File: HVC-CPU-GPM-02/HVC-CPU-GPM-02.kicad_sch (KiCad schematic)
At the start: 31 parts, among them P1 CART, P3 RF, P6 POWER, Q1 2SA937, SW1 RESET, U1 MB8416, U2 74LS373, U3 74LS139, U4 MB8416, U5 RP2C02, U6 RP2A03

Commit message: Refactor schematic: * Move audio and video circuits to dedicated sheet * Move power and mechanical to dedicated sheet Modify P1 Cart Connector symbol to: * split out audio ports * organize pins for easier wiring Modify 74LS346 symbol: * Split A/B ports to allow moving functions to related circuits Modify X1 crystal footprint: * change from stock footprint to custom footprint Correct crystal name from Y1 to X1
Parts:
- removed C10, C35: 0.01u, Nintendo:C_Disc_D3.0mm_W2.0mm_P3.0mm, symbol Device:C
- removed C34, C40, C41, C42, C43, C44, C45, C46: 330p, Nintendo:C_Disc_D3.0mm_W2.0mm_P3.0mm, symbol Device:C
- removed C8: 0.47u, Capacitor_THT:CP_Radial_D5.0mm_P2.50mm, symbol Device:C_Polarized
- removed FC1: 39u, Inductor_THT:L_Axial_L5.0mm_D3.6mm_P10.00mm_Horizontal_Murata_BL01RN1A2A2, symbol Device:L_Ferrite
- removed FC2: FerriteBead, Inductor_THT:L_Axial_L5.0mm_D3.6mm_P10.00mm_Horizontal_Murata_BL01RN1A2A2, symbol Device:FerriteBead
- removed H1: Top Left, Nintendo:npth_mounting_4x5mm_pad, symbol Mechanical:MountingHole_Pad
- removed H2: Top Right, Nintendo:npth_mounting_4x5mm_nopad, symbol Mechanical:MountingHole
- removed H3: Bottom Left, Nintendo:npth_mounting_3.3x5mm_nopad, symbol Mechanical:MountingHole
- removed H4: Bottom Right, Nintendo:npth_mounting_3.3x5mm_nopad, symbol Mechanical:MountingHole
- removed H5: Alignment, Nintendo:npth_mounting_2x4mm_nopad, symbol Mechanical:MountingHole
- removed P6: POWER, Nintendo:connector_P6_2pin, symbol Switch:SW_SPST
- removed Q1: 2SA937, Nintendo:PACKAGE_TRANSISTOR_FTR, symbol Simulation_SPICE:PNP
- removed R6: 150, Resistor_THT:R_Axial_DIN0207_L6.3mm_D2.5mm_P10.16mm_Horizontal, symbol Device:R
- removed SW1: RESET, Nintendo:switch_reset_9x10_4pin, symbol Switch:SW_Push_Dual
- removed unit 3 of U3
- added C37, C38: 560p, Nintendo:C_Disc_D3.0mm_W2.0mm_P3.0mm, symbol Device:C
- P1: value CART -> CARTRIGE SLOT
- P3: value RF -> RF MODULATOR; symbol Connector:Conn_01x05_Socket -> Famicom:RF_MODULATOR
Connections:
- net GND: now also C37.2, C38.2
- net SOUND+CART: no longer P1.46 (SNDO)
- net ~{INP0}: now also C38.1
- net ~{INP1}: now also C37.1
- net AUDIO renamed RF_AUDIO
- net Clock/CPU_CLK renamed CPU_CLK
- net Clock/PPU_CLK renamed PPU_CLK
- net POWER_IN renamed POWER
- net SND1 renamed CPU_SND1
- net SND2 renamed CPU_SND2
- removed net SOUND: P1.45 (SNDI)
- net VIDEO renamed PPU_VIDEO
- net VID_AF renamed RF_VIDEO
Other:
- sheet Audio renamed Audio and Video
- added sheet Power and Mechanical (power_mech.kicad_sch)
- sheet Audio and Video ports: added CPU_SND1, CPU_SND2, MIC, PA13, PPU_VIDEO, RF_AUDIO, RF_VIDEO, SOUND+CART, ~{PA13}; removed none
- sheet Controllers ports: added none; removed PA13, SND1, SND2, SOUND, ~{PA13}
- note added: "1 2 3 4 5 6 7 8 9 10 11 12 13 14 15 16 17 18 19 20 21 22 23 24 25 26 27 28 29 30"
- note added: "31 32 33 34 35 36 37 38 39 40 41 42 43 44 45 46 47 48 49 50 51 52 53 54 55 56 57 58 59 60"
- note added: "ADDRESS LATCH"
- note added: "CPU"
- note added: "GND A11 A10 A9 A8 A7 A6 A5 A4 A3 A2 A1 A0 R/~{W} ~{IRQ} GND ~{RD} VA10 PA6 PA5 PA4 PA3 PA2 PA1 PA0 PD0 PD1 PD2 PD3 VCC"
- note added: "POWER"
- note added: "RESET"
- note added: "RF_VCC M2 A12 A13 A14 D7 D6 D5 D4 D3 D2 D1 D0 ~{ROMSEL} SNDI SNDO ~{WE} ~{VCS} ~{PA13} PA7 PA8 PA9 PA10 PA11 PA12 PA13 PD7 PD6 PD5 PD4"
- note removed: "INDUCTORS 39uH x1 Ferrite x1"
- moved on the sheet: RM1F, RM1G, U1, U2, U3A, U3B, U4, U5, U6

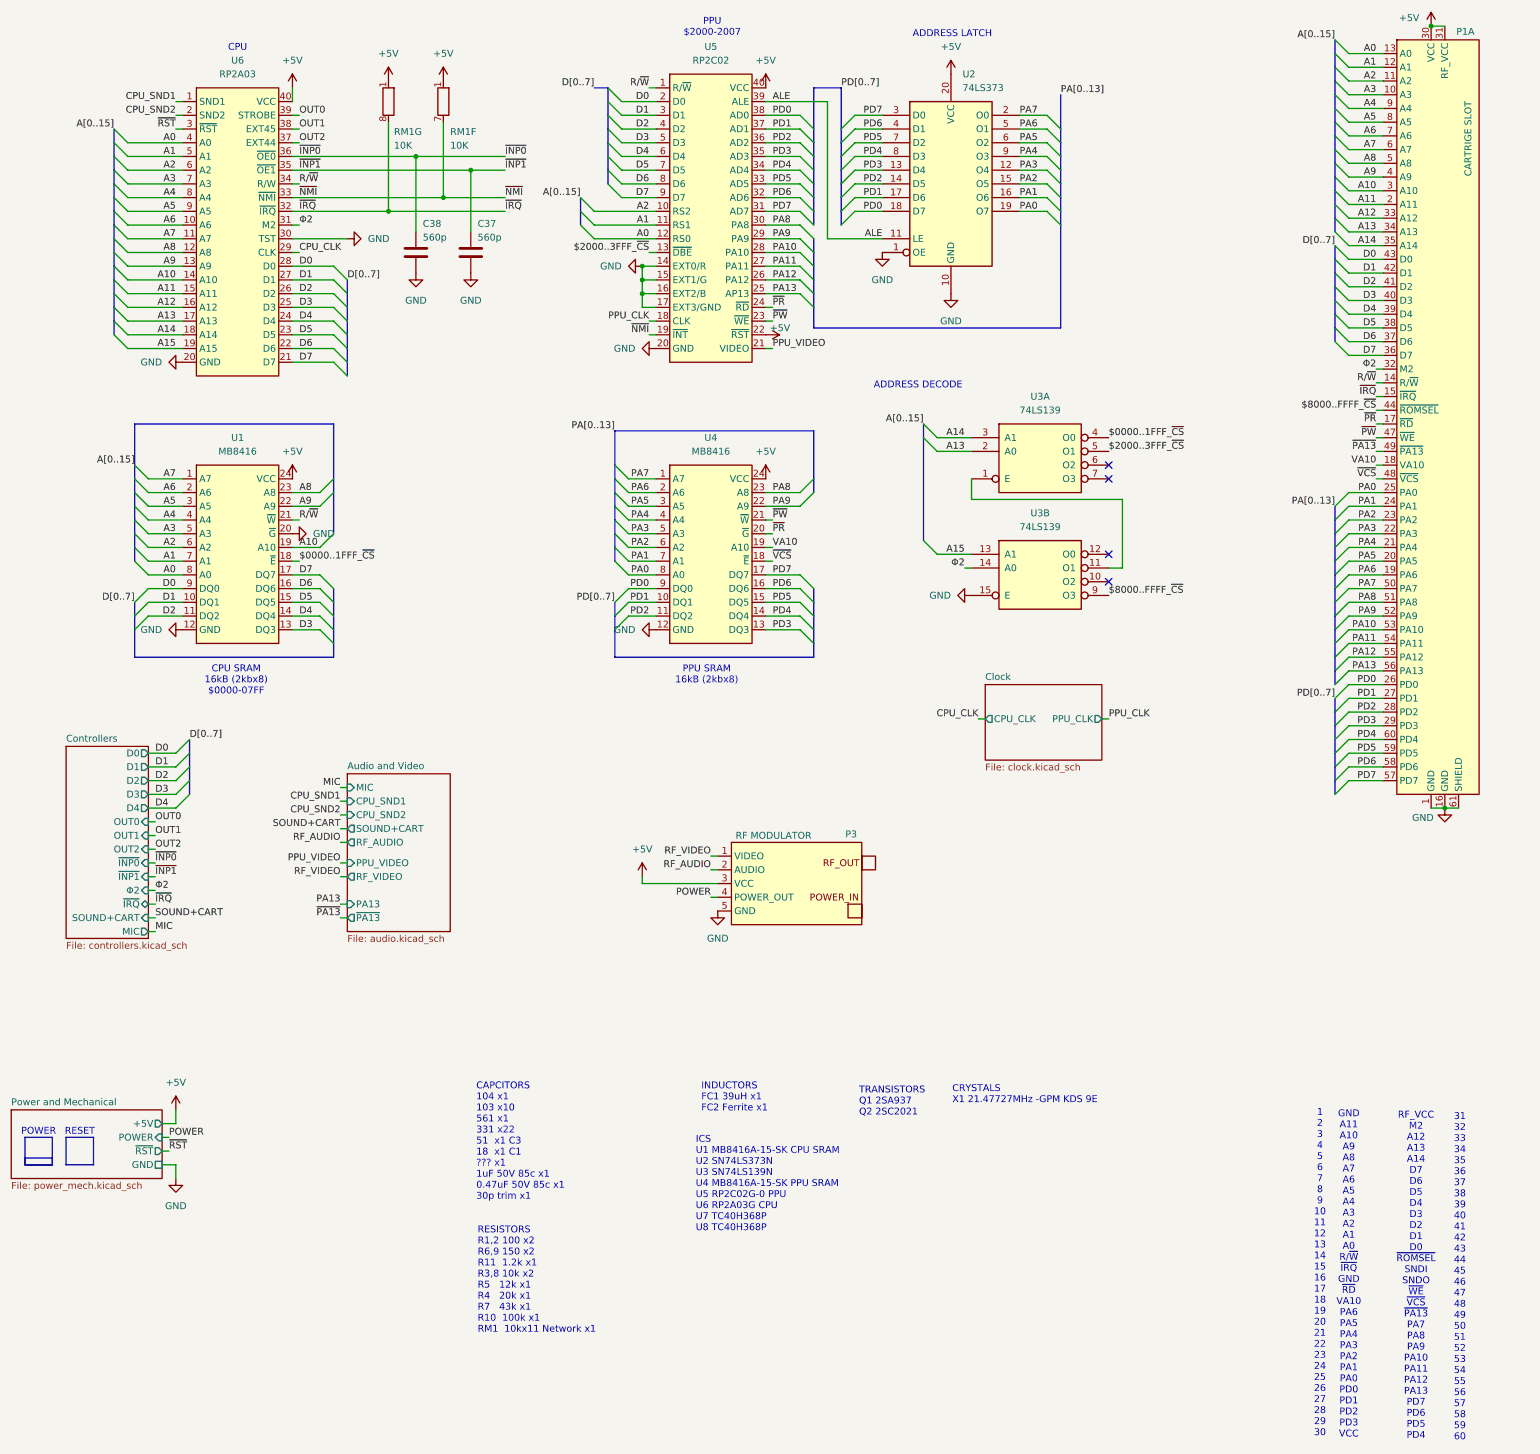
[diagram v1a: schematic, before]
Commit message: Change symbols to functional layout instead of pin map layout Add technical page to store pinouts Organize and compact root page
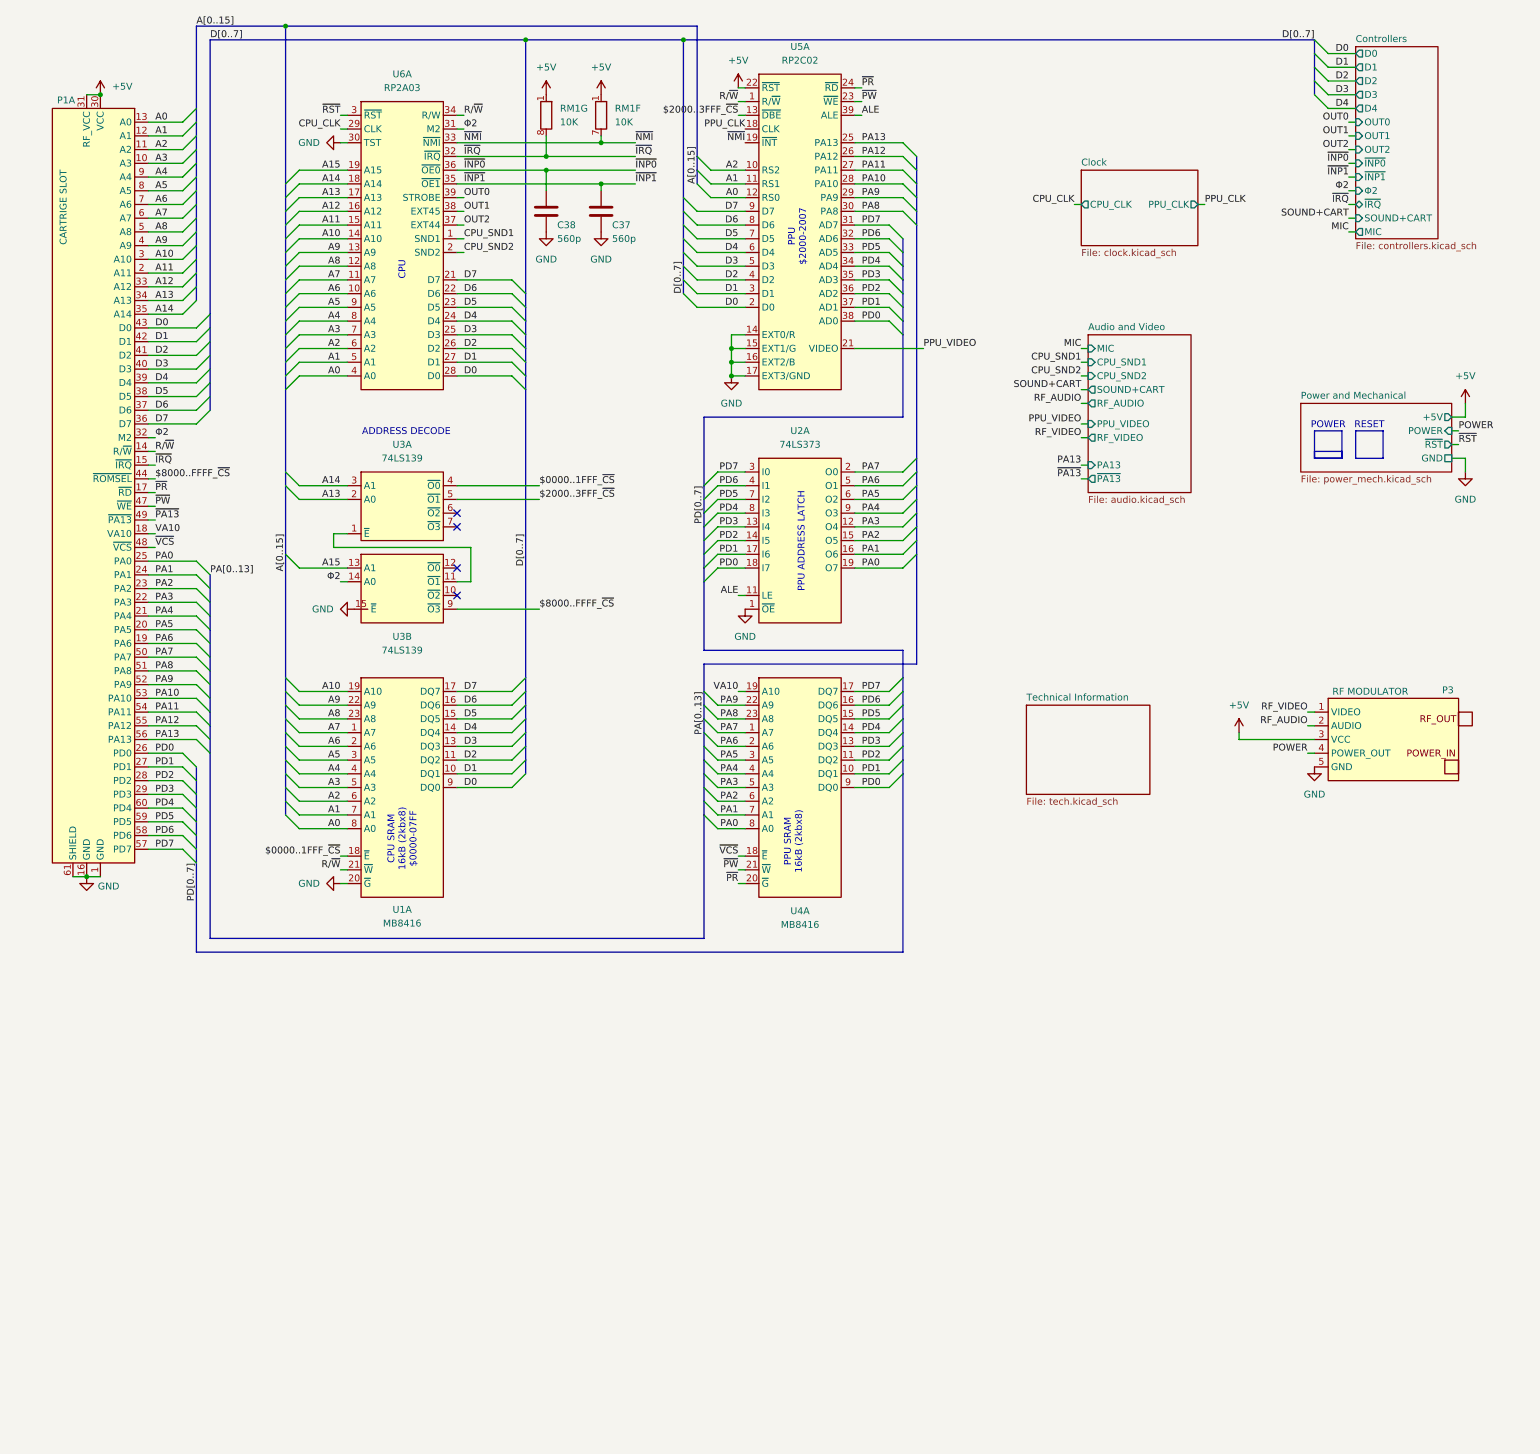
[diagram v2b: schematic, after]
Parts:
- U2: symbol 74xx:74LS373 -> Famicom:74LS373
- U3: symbol 74xx:74LS139 -> Famicom:74LS139
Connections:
- net +5V: no longer U1.24 (VCC), U2.20 (VCC), U4.24 (VCC), U5.40 (VCC), U6.40 (VCC)
- net GND: no longer U1.12 (GND), U2.10 (GND), U4.12 (GND), U5.20 (GND), U6.20 (GND)
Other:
- added sheet Technical Information (tech.kicad_sch)
- note added: "PPU ADDRESS LATCH"
- note removed: "1 2 3 4 5 6 7 8 9 10 11 12 13 14 15 16 17 18 19 20 21 22 23 24 25 26 27 28 29 30"
- note removed: "31 32 33 34 35 36 37 38 39 40 41 42 43 44 45 46 47 48 49 50 51 52 53 54 55 56 57 58 59 60"
- note removed: "ADDRESS LATCH"
- note removed: "CAPCITORS 104 x1 103 x10 561 x1 331 x22 51 x1 C3 18 x1 C1 ??? x1 1uF 50V 85c x1 0.47uF 50V 85c x1 30p trim x1"
- note removed: "CRYSTALS X1 21.47727MHz -GPM KDS 9E"
- note removed: "GND A11 A10 A9 A8 A7 A6 A5 A4 A3 A2 A1 A0 R/~{W} ~{IRQ} GND ~{RD} VA10 PA6 PA5 PA4 PA3 PA2 PA1 PA0 PD0 PD1 PD2 PD3 VCC"
- note removed: "ICS U1 MB8416A-15-SK CPU SRAM U2 SN74LS373N U3 SN74LS139N U4 MB8416A-15-SK PPU SRAM U5 RP2C02G-0 PPU U6 RP2A03G CPU U7 TC40H368P U8 TC40H368P"
- note removed: "INDUCTORS FC1 39uH x1 FC2 Ferrite x1"
- note removed: "RESISTORS R1,2 100 x2 R6,9 150 x2 R11 1.2k x1 R3,8 10k x2 R5 12k x1 R4 20k x1 R7 43k x1 R10 100k x1 RM1 10kx11 Network x1"
- note removed: "RF_VCC M2 A12 A13 A14 D7 D6 D5 D4 D3 D2 D1 D0 ~{ROMSEL} SNDI SNDO ~{WE} ~{VCS} ~{PA13} PA7 PA8 PA9 PA10 PA11 PA12 PA13 PD7 PD6 PD5 PD4"
- note removed: "TRANSISTORS Q1 2SA937 Q2 2SC2021"
- moved on the sheet: C37, C38, P1A, P3, RM1F, RM1G

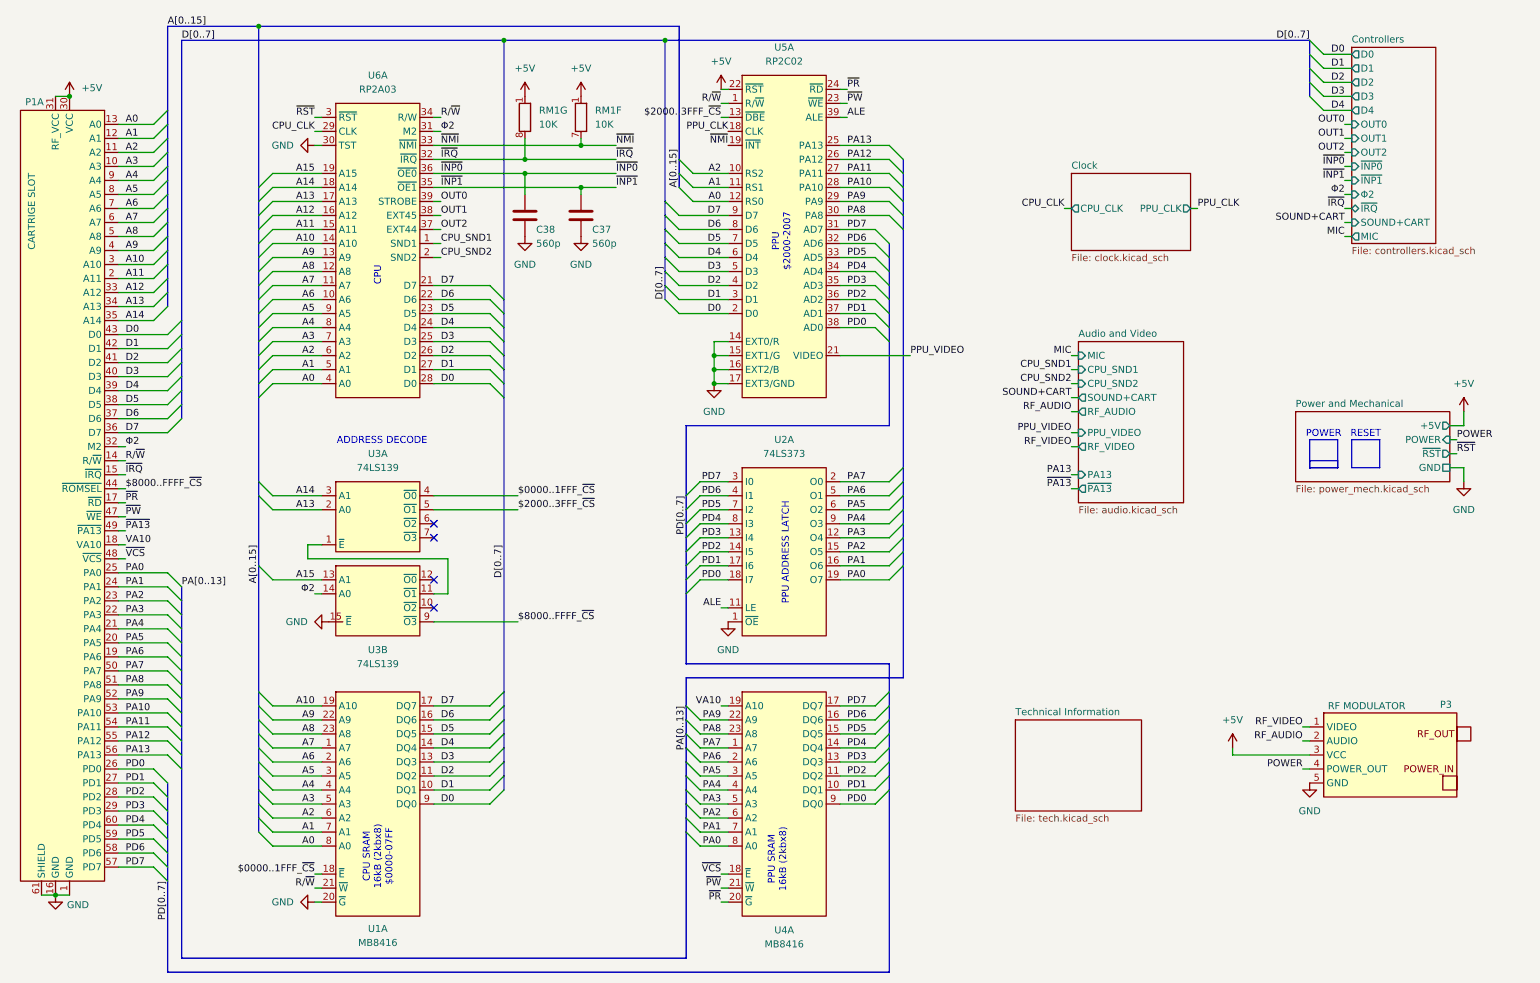
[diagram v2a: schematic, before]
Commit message: Rearranged pins on some symbols to simplify schematic wiring Removed schematics for controller PCBs Added PNG version of schematics
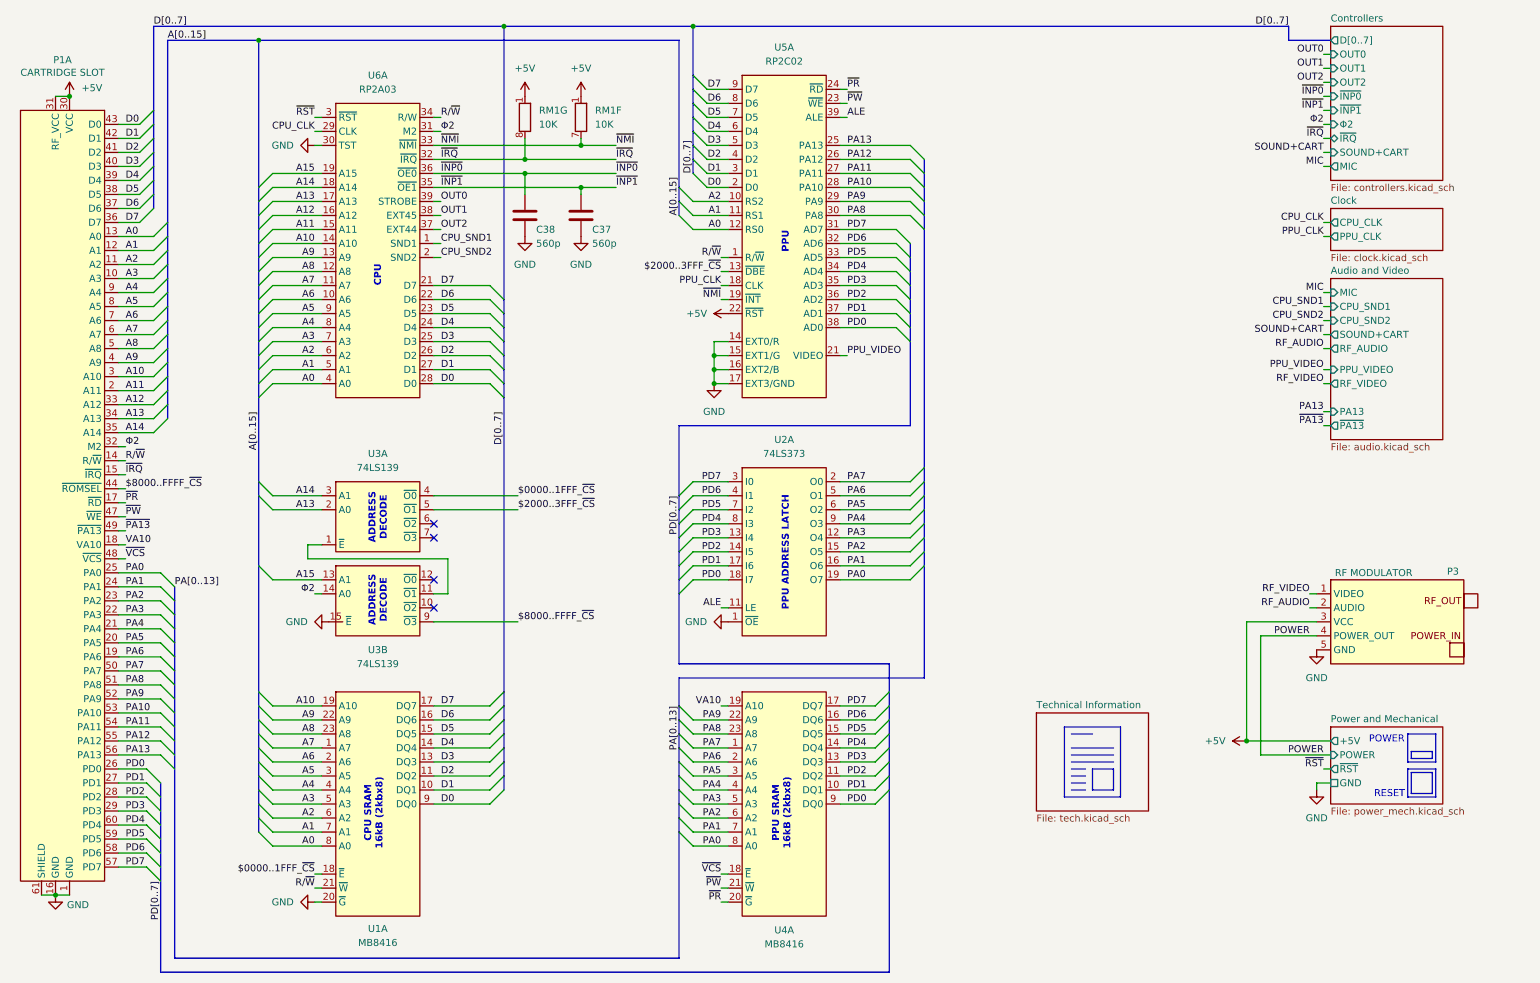
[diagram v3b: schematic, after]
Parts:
- P1: value CARTRIGE SLOT -> CARTRIDGE SLOT
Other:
- sheet Controllers ports: added D[0..7]; removed D0, D1, D2, D3, D4
- note added: "CPU SRAM 16kB (2kbx8)"
- note added: "PPU"
- note removed: "CPU SRAM 16kB (2kbx8) $0000-07FF"
- note removed: "PPU $2000-2007"
- title: (none) -> Nintendo Famicom Mainboard
- moved on the sheet: P3
